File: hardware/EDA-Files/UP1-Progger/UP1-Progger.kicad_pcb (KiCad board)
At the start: 2 copper layers, 27.9 x 31.8 mm, 11 parts, among them J1 KUPS-Conn, J2 USB_B_Micro, J3 USB_B, J4 SWD_Interface, J5 ST Link V2 Clone, J6 USB_2.54, SW1 Reset, SW2 Bootsel, U1 LDO_3V3_SOT23-3

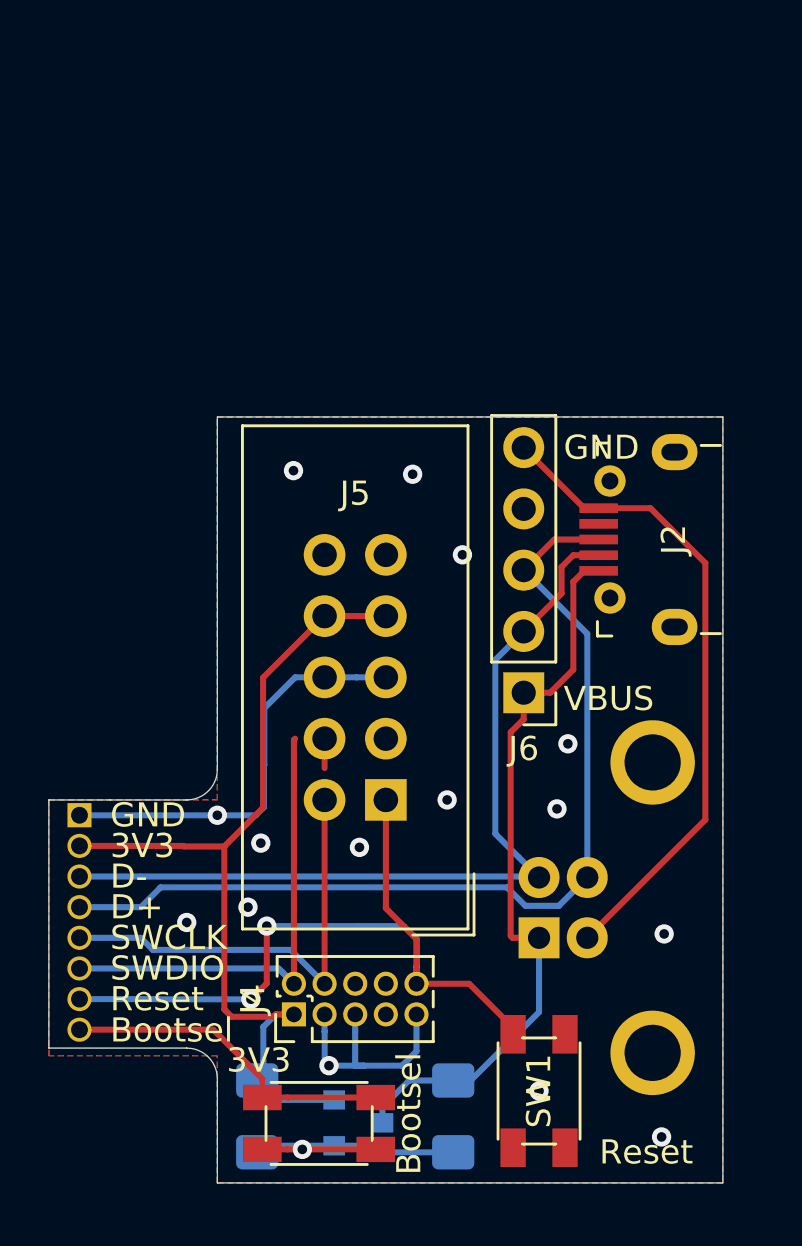
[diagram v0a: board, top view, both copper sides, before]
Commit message: made one-sided Progger ready for SMT assembly of USB and LDO V00.20 - not released
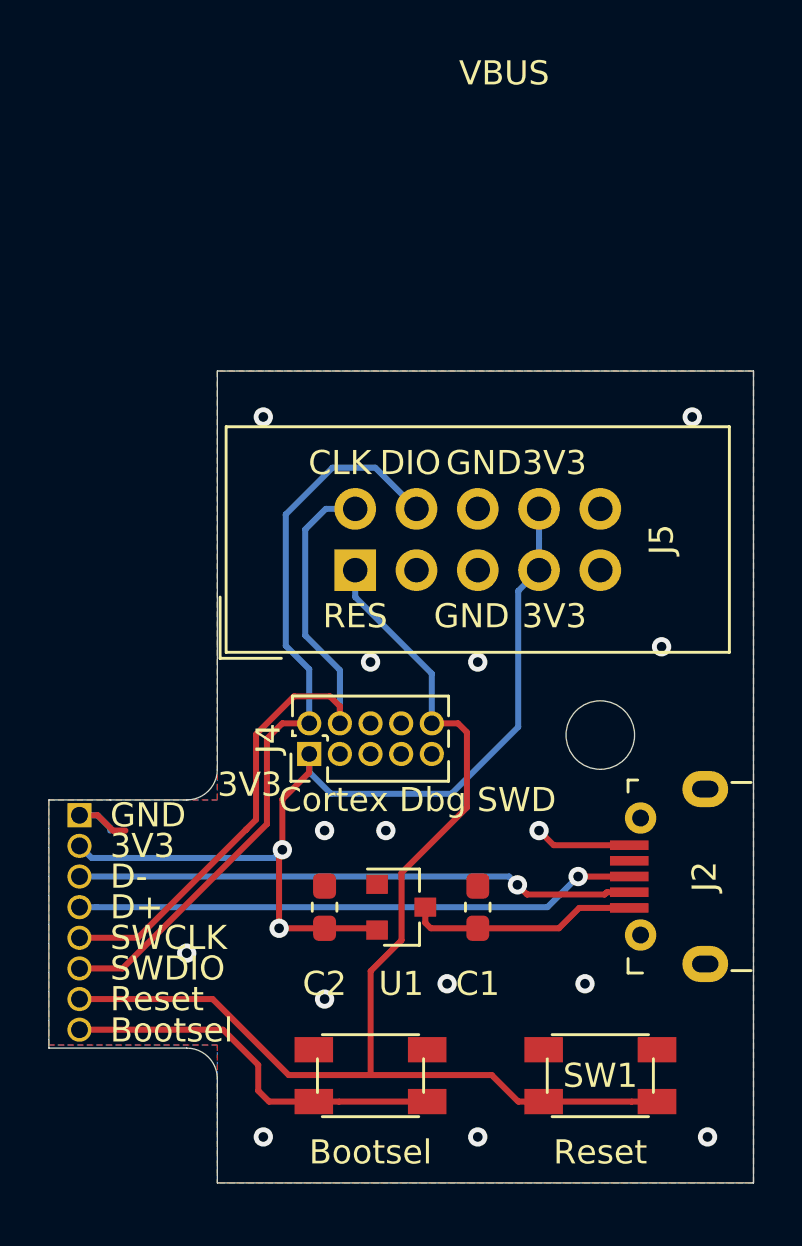
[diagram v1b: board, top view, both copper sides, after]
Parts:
- removed J3: USB_B, sirsydom:USB_B_OST_USB-B1HSxx_Horizontal
- removed J6: USB_2.54, Connector_PinHeader_2.54mm:PinHeader_1x05_P2.54mm_Vertical
- added G***: LOGO, OpenKNX:OpenKNX_Logo_14x09, B.Cu at (103.5, 116.8)
- C1, C2: footprint Capacitor_SMD:C_1206_3216Metric_Pad1.42x1.75mm_HandSolder -> Capacitor_SMD:C_0603_1608Metric_Pad1.05x0.95mm_HandSolder; moved to F.Cu
- U1: moved to F.Cu
- moved J2 14.0 mm to (119.4, 115.6)
- moved J4 10.8 mm to (101.0, 110.5)
- moved J5 9.61 mm to (102.9, 102.9), turned to 90 degrees
- moved U1 9.12 mm to (104.8, 116.8)
- moved C2 9.11 mm to (101.6, 116.8), turned to 90 degrees
- moved C1 8.73 mm to (108.0, 116.8), turned to 90 degrees
- moved SW2 2.91 mm to (103.5, 123.8), turned to 0 degrees
- moved SW1 2.62 mm to (113.0, 123.8), turned to 0 degrees
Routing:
- net GND: track 67.9 -> 7.76 mm, vias 16 -> 15
- net +5V: track 31.0 -> 9.55 mm
- net Reset: track 31.9 -> 50.8 mm, vias 2 -> 0
- net D+: track 39.7 -> 23.3 mm, vias 0 -> 1
- net D-: track 35.6 -> 23.1 mm, vias 0 -> 1
- net SWDIO: track 21.3 -> 31.8 mm
- net SWCLK: track 18.6 -> 29.1 mm
- net +3V3: track 36.9 -> 40.9 mm, vias 0 -> 2
- net Bootsel: track 13.9 -> 16.3 mm
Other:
- board size 27.9 x 31.8 mm -> 29.2 x 33.7 mm
- board text added: "CLK"
- board text added: "Cortex Dbg SWD"
- board text added: "DIO"
- board text added: "RES"
- board text added: "UP1-Progger"
- board text added: "V00.20"
- board text removed: "OpenKNX.de UP1-Progger"
- board text removed: "V00.10"
